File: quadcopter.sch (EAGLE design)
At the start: 0 parts

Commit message: Beginning to copy red board design
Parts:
- added C1: 1uF, quadparts_prebuilt:CAPACITOR-NP_SMD-2012-0805_CERAMIC-1UF
- added C4: 100uF, quadparts_prebuilt:CAPACITOR-POL_SMD-7043-D_TANTALUM-220UF
- added D1: 20V-500MA, quadparts_prebuilt:DIODE-SCHOTTKY_SMD-SOD123
- added R1, R2: 10K, quadparts_prebuilt:RESISTOR_SMD-2012-0805-10K
- added U$1: MOTOR_PADS, quadparts_prebuilt:MOTOR_PADS
- added U$2: MOSFET_20V, quadparts:MOSFET_20V
- added U1: ATMEGA128RFA1, quadparts_prebuilt:ATMEGA128RFA1
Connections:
- new net FILTERED: R1.2, R2.2, U$2.P-G
- new net FLYBACK: D1.A, U$1.V-, U$2.P-D
- new net GND: C1.2, C4.-, R2.1, U$2.P-S
- new net MISO: U1.PB3(MISO/PDO/PCINT3)
- new net MOSI: U1.PB2(MOSI/PDI/PCINT2)
- new net N$1: U1.EVDD
- new net N$10: U1.AVDD
- new net N$11: U1.DVDD
- new net N$12: U1.XTAL1
- new net N$13: U1.XTAL2
- new net N$14: U1.CLKI
- new net N$15: U1.AREF
- new net N$16: U1.PF0(ADC0)
- new net N$17: U1.PF1(ADC1)
- new net N$18: U1.PF2(ADC2/DIG2)
- new net N$19: U1.PF3(ADC3/DIG4)
- new net N$2: U1.DEVDD
- new net N$20: U1.PF4(ADC4/TCK)
- new net N$21: U1.PF5(ADC5/TMS)
- new net N$22: U1.PF6(ADC6/TDO)
- new net N$23: U1.PF7(ADC7/TDI)
- new net N$24: U1.AVSS
- new net N$25: U1.DVSS
- new net N$3: U1.RSTN
- new net N$4: U1.RSTON
- new net N$46: U1.PE4(OC3B/INT4)
- new net N$48: U1.PE6(T3/INT6)
- new net N$49: U1.PE7(ICP3/INT7/CLKO)
- new net N$5: U1.TST
- new net N$50: U1.PG0(DIG3)
- new net N$51: U1.PG1(DIG1)
- new net N$52: U1.PG2(AMR)
- new net N$53: U1.PG3(TOSC2)
- new net N$54: U1.PG4(TOSC1)
- new net N$55: U1.PG5(OC0B)
- new net N$6: U1.RFP
- new net N$7: U1.RFN
- new net N$8: U1.AVSS_RFP
- new net N$9: U1.AVSS_RFN
- new net PB4: U1.PB4(OC2A/PCINT4)
- new net PB5: U1.PB5(OC1A/PCINT5)
- new net PB6: U1.PB6(OC1B/PCINT6)
- new net PB7: U1.PB7(OC0A/OC1C/PCINT7)
- new net PD4: U1.PD4(ICP1)
- new net PD5: U1.PD5(XCK1)
- new net PD6: U1.PD6(T1)
- new net PD7: U1.PD7(T0)
- new net PE2: U1.PE2(XCK0/AIN0)
- new net PE3: U1.PE3(OC3A/AIN1)
- new net PE4: U1.PE5(OC3C/INT5)
- new net PWM: C1.1, R1.1
- new net RX0: U1.PE0(RXD0/PCINT8)
- new net RX1: U1.PD2(RXD1/INT2)
- new net SCK: U1.PB1(SCK/PCINT1)
- new net SCL: U1.PD0(SCL/INT0)
- new net SDA: U1.PD1(SDA/INT1)
- new net SSN: U1.PB0(SSN/PCINT0)
- new net TX0: U1.PE1(TXD0)
- new net TX1: U1.PD3(TXD1/INT3)
- new net VCC: C4.+, D1.C, U$1.V+
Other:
- note added: "Filter"
- note added: "Flyback"

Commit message: Added necessary components from red board design
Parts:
- added B1: BALUN0805, quadparts_prebuilt:BALUN0805
- added C10: 0.75pF, quadparts_prebuilt:CAPACITOR-NP_SMD-2012-0805_CERAMIC-0.75PF
- added C11, C12, C7, C8: 1uF, quadparts_prebuilt:CAPACITOR-NP_SMD-2012-0805_CERAMIC-1UF
- added C13: 0.1uF, quadparts_prebuilt:CAPACITOR-NP_SMD-2012-0805_CERAMIC-0.1UF
- added C2, C3, C5, C6: 12pF, quadparts_prebuilt:CAPACITOR-NP_SMD-2012-0805_CERAMIC-12PF
- added C9: 22pF, quadparts_prebuilt:CAPACITOR-NP_SMD-2012-0805_CERAMIC-22PF
- added D2, D3: green, quadparts_prebuilt:DIODE-LED_SMD-2012-0805-GREEN
- added J1: AVR_SPI_PRG_6NS, quadparts_prebuilt:AVR_SPI_PRG_6NS
- added JP1: FTDI_BASICPTH, quadparts_prebuilt:FTDI_BASICPTH
- added R3, R4: 330, quadparts_prebuilt:RESISTOR_SMD-2012-0805-330
- added R5: 10K, quadparts_prebuilt:RESISTOR_SMD-2012-0805-10K
- added U$3: ANTENNA2SMD5, quadparts_prebuilt:ANTENNA2SMD5
- added Y1: 32.768kHz, quadparts_prebuilt:CRYSTAL5X3
- added Y2: 16MHz, quadparts_prebuilt:CRYSTAL5X3
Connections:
- net N$14 renamed CLKI
- net N$15 renamed AREF
- net N$16 renamed A0
- net N$17 renamed A1
- net N$18 renamed A2
- net N$19 renamed A3
- net N$20 renamed A4
- net N$21 renamed A5
- net N$22 renamed A6
- net N$23 renamed A7
- net N$4 renamed RSTON
- net N$48 renamed PE6
- net N$49 renamed PE7
- net N$5 renamed TST
- net N$50 renamed PG0
- net N$51 renamed PG1
- net N$52 renamed PG2
- net N$55 renamed PG5
- removed net N$24: U1.AVSS
- removed net N$25: U1.DVSS
- removed net N$46: U1.PE4(OC3B/INT4)
- removed net N$53: U1.PG3(TOSC2)
- removed net N$54: U1.PG4(TOSC1)
- removed net VCC: C4.+, D1.C, U$1.V+
- new net 3V: C11.1, C12.1, C4.+, D1.C, J1.2, R5.2, U$1.V+, U1.DEVDD, U1.EVDD
- new net N$14: J1.1
- new net N$15: J1.3
- new net N$16: J1.5
- new net N$19: J1.6
- new net N$4: C5.1, U1.XTAL2, Y2.2
- new net N$5: C6.1, U1.XTAL1, Y2.1
- new net PE5: U1.PE5(OC3C/INT5)
- new net RESET: C13.2, R5.1, U1.RSTN
- net GND: now also B1.GND@5, C10.2, C11.2, C12.2, C2.2, C3.2, C5.2, C6.2, C7.2, C8.2, C9.2, D2.C, D3.C, JP1.6, U1.AVSS, U1.AVSS_RFN, U1.AVSS_RFP, U1.DVSS
- net MOSI: now also J1.4
- net N$1: now also C2.1, U1.PG4(TOSC1), Y1.1; no longer U1.EVDD
- net N$10: now also B1.OUT2, U1.RFN; no longer U1.AVDD
- net N$11: now also B1.GND@2, C9.1; no longer U1.DVDD
- net N$12: now also B1.IN, C10.1, U$3.SIGNAL; no longer U1.XTAL1
- net N$13: now also C13.1, JP1.1; no longer U1.XTAL2
- net N$2: now also C3.1, U1.PG3(TOSC2), Y1.2; no longer U1.DEVDD
- net N$3: now also D2.A, R3.1; no longer U1.RSTN
- net N$6: now also D3.A, R4.1; no longer U1.RFP
- net N$7: now also C7.1, U1.DVDD; no longer U1.RFN
- net N$8: now also C8.1, U1.AVDD; no longer U1.AVSS_RFP
- net N$9: now also B1.OUT1, U1.RFP; no longer U1.AVSS_RFN
- net PB6: now also R4.2
- net PB7: now also R3.2
- net PE4: now also U1.PE4(OC3B/INT4); no longer U1.PE5(OC3C/INT5)
- net RX0: now also JP1.3
- net TX0: now also JP1.2
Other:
- moved on the sheet: C1, C4, D1, R1, R2, U$1, U$2, U1

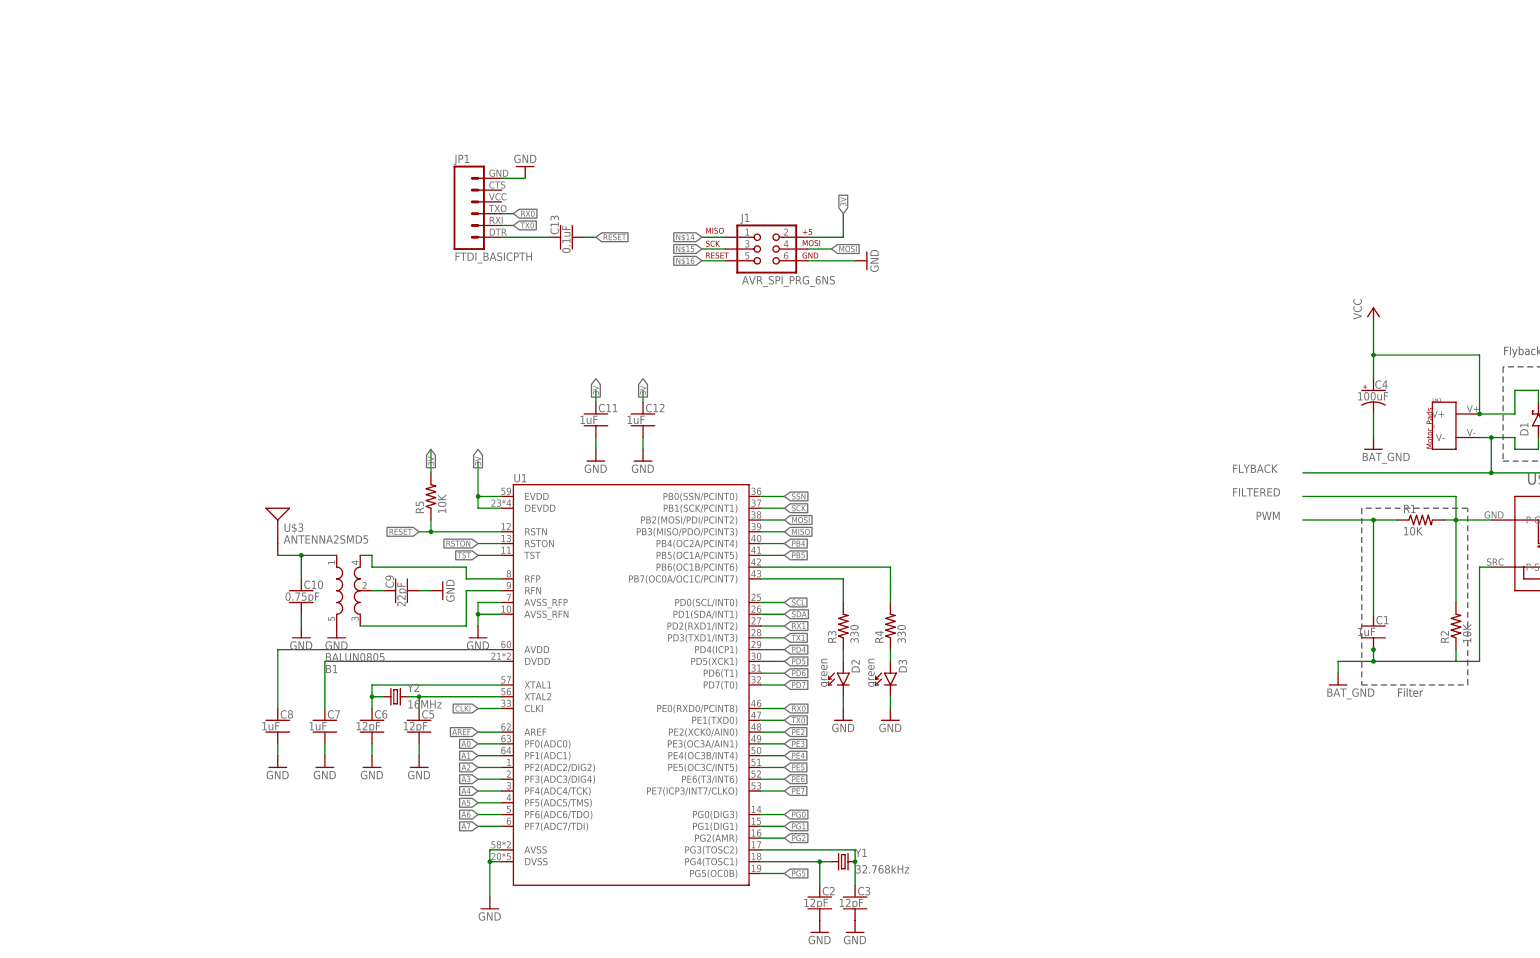
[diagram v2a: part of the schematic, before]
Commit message: Added power supply, FTDI and debugging headers, misc. fixes.
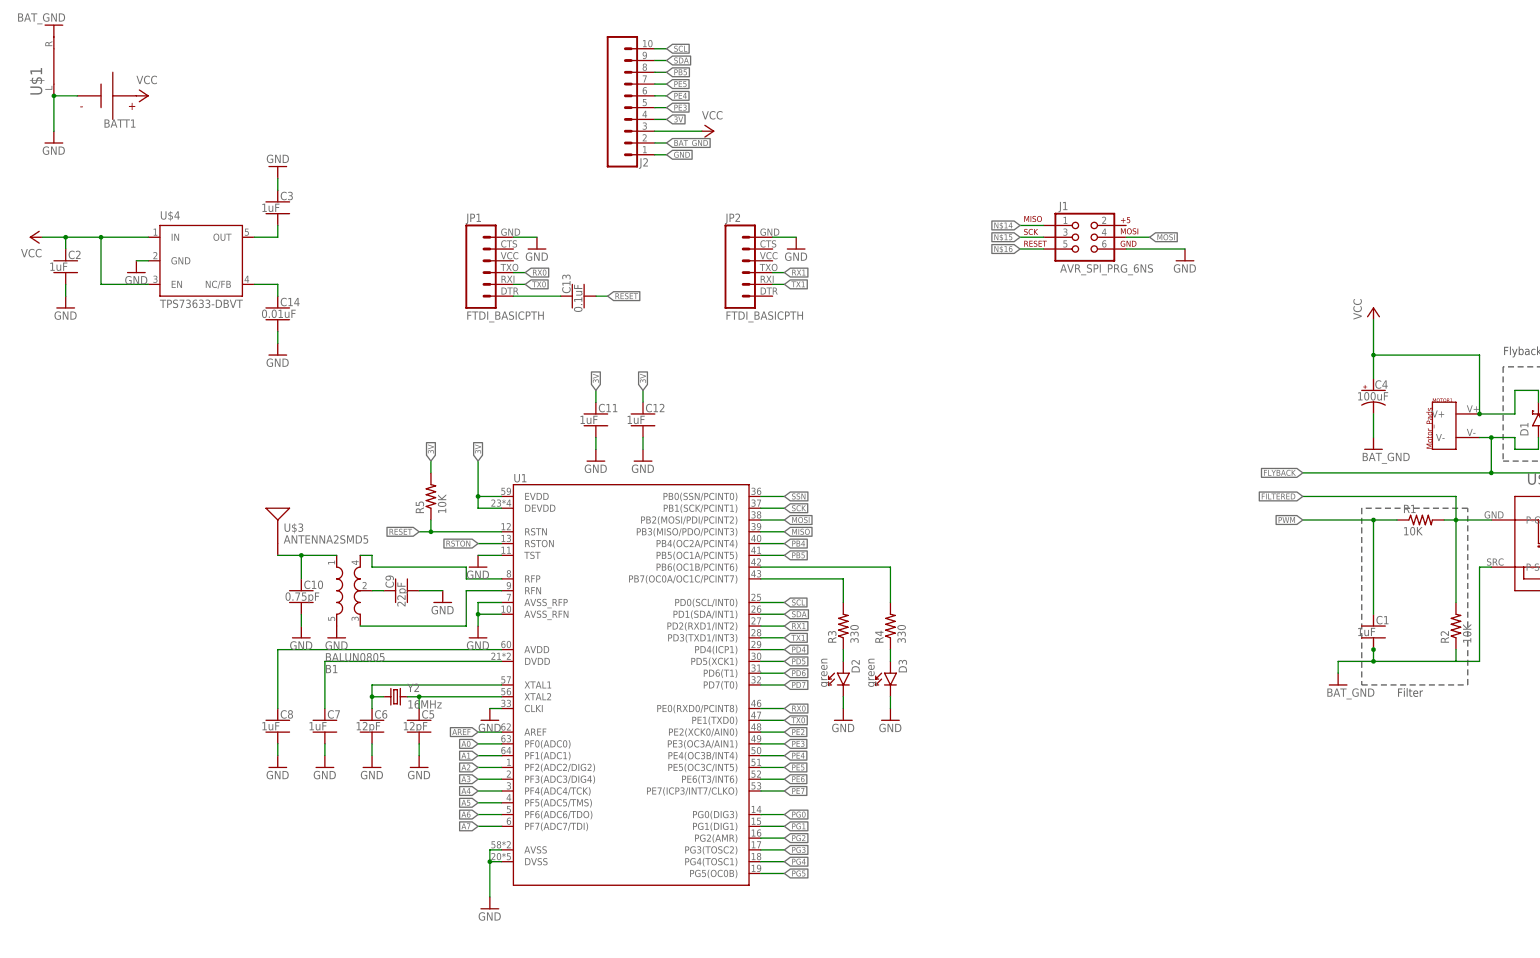
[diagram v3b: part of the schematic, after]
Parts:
- removed Y1: 32.768kHz, quadparts_prebuilt:CRYSTAL5X3
- added BATT1: BATTERY-HUBSAN-W/HOLDER, quadparts_prebuilt:BATTERY-HUBSAN-W/HOLDER
- added C14: 0.01uF, quadparts_prebuilt:CAPACITOR-NP_SMD-2012-0805_CERAMIC-0.01UF
- added J2: (no value), quadparts_prebuilt:SIP-10_TH-254X10
- added JP2: FTDI_BASICPTH, quadparts_prebuilt:FTDI_BASICPTH
- added MOTOR1: MOTOR_PADS, quadparts_prebuilt:MOTOR_PADS
- added U$4: TPS73633-DBVT, quadparts_prebuilt:TPS73633-DBVT
- C2, C3: value 12pF -> 1uF; device quadparts_prebuilt:CAPACITOR-NP_SMD-2012-0805_CERAMIC-12PF -> quadparts_prebuilt:CAPACITOR-NP_SMD-2012-0805_CERAMIC-1UF
- U$1: value MOTOR_PADS -> NET_BRIDGE; device quadparts_prebuilt:MOTOR_PADS -> quadparts:NET_BRIDGE
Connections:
- removed net CLKI: U1.CLKI
- removed net N$19: J1.6
- removed net TST: U1.TST
- new net BAT_GND: J2.2, U$1.R
- new net PG3: U1.PG3(TOSC2)
- new net PG4: U1.PG4(TOSC1)
- new net VCC: BATT1.P, C2.1, J2.3, U$4.EN, U$4.IN
- net 3V: now also J2.4, MOTOR1.V+; no longer J1.2, U$1.V+
- net FLYBACK: now also MOTOR1.V-; no longer U$1.V-
- net GND: now also BATT1.N, C14.2, C3.1, J1.6, J2.1, JP2.6, U$1.L, U$4.GND, U1.CLKI, U1.TST; no longer C3.2
- net N$1: now also C14.1, U$4.NC/FB; no longer C2.1, U1.PG4(TOSC1), Y1.1
- net N$2: now also C3.2, U$4.OUT; no longer C3.1, U1.PG3(TOSC2), Y1.2
- net PB5: now also J2.8
- net PE3: now also J2.5
- net PE4: now also J2.6
- net PE5: now also J2.7
- net RX1: now also JP2.3
- net SCL: now also J2.10
- net SDA: now also J2.9
- net TX1: now also JP2.2
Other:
- moved on the sheet: C13, C2, C3, J1, JP1

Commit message: Added battery disconnect, replicated motor controller w/ pwm, misc fixes.
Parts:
- added C15, C17, C19: 1uF, quadparts_prebuilt:CAPACITOR-NP_SMD-2012-0805_CERAMIC-1UF
- added C16, C18, C20: 100uF, quadparts_prebuilt:CAPACITOR-POL_SMD-7043-D_TANTALUM-220UF
- added D4, D5, D6: 20V-500MA, quadparts_prebuilt:DIODE-SCHOTTKY_SMD-SOD123
- added J3: (no value), quadparts:MALE_HEADER_2POS-2X1-0.1IN
- added MOTOR2, MOTOR3, MOTOR4: MOTOR_PADS, quadparts_prebuilt:MOTOR_PADS
- added R10, R11, R6, R7, R8, R9: 10K, quadparts_prebuilt:RESISTOR_SMD-2012-0805-10K
- added U$5, U$6, U$7: MOSFET_20V, quadparts:MOSFET_20V
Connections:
- removed net N$2: C3.2, U$4.OUT
- removed net PWM: C1.1, R1.1
- new net N$17: BATT1.P, J3.1
- net 3V: now also C16.+, C18.+, C20.+, C3.2, D4.C, D5.C, D6.C, MOTOR2.V+, MOTOR3.V+, MOTOR4.V+, U$4.OUT
- net FILTERED: now also R10.2, R11.2, R6.2, R7.2, R8.2, R9.2, U$5.P-G, U$6.P-G, U$7.P-G
- net FLYBACK: now also D4.A, D5.A, D6.A, MOTOR2.V-, MOTOR3.V-, MOTOR4.V-, U$5.P-D, U$6.P-D, U$7.P-D
- net GND: now also C15.2, C16.-, C17.2, C18.-, C19.2, C20.-, R11.1, R7.1, R9.1, U$5.P-S, U$6.P-S, U$7.P-S
- net PB5: now also C15.1, R6.1
- net PE3: now also C1.1, R1.1
- net PE4: now also C19.1, R10.1
- net PE5: now also C17.1, R8.1
- net VCC: now also J3.2; no longer BATT1.P
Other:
- moved on the sheet: B1, C1, C10, C11, C12, C4, C5, C6, C7, C8, C9, D1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

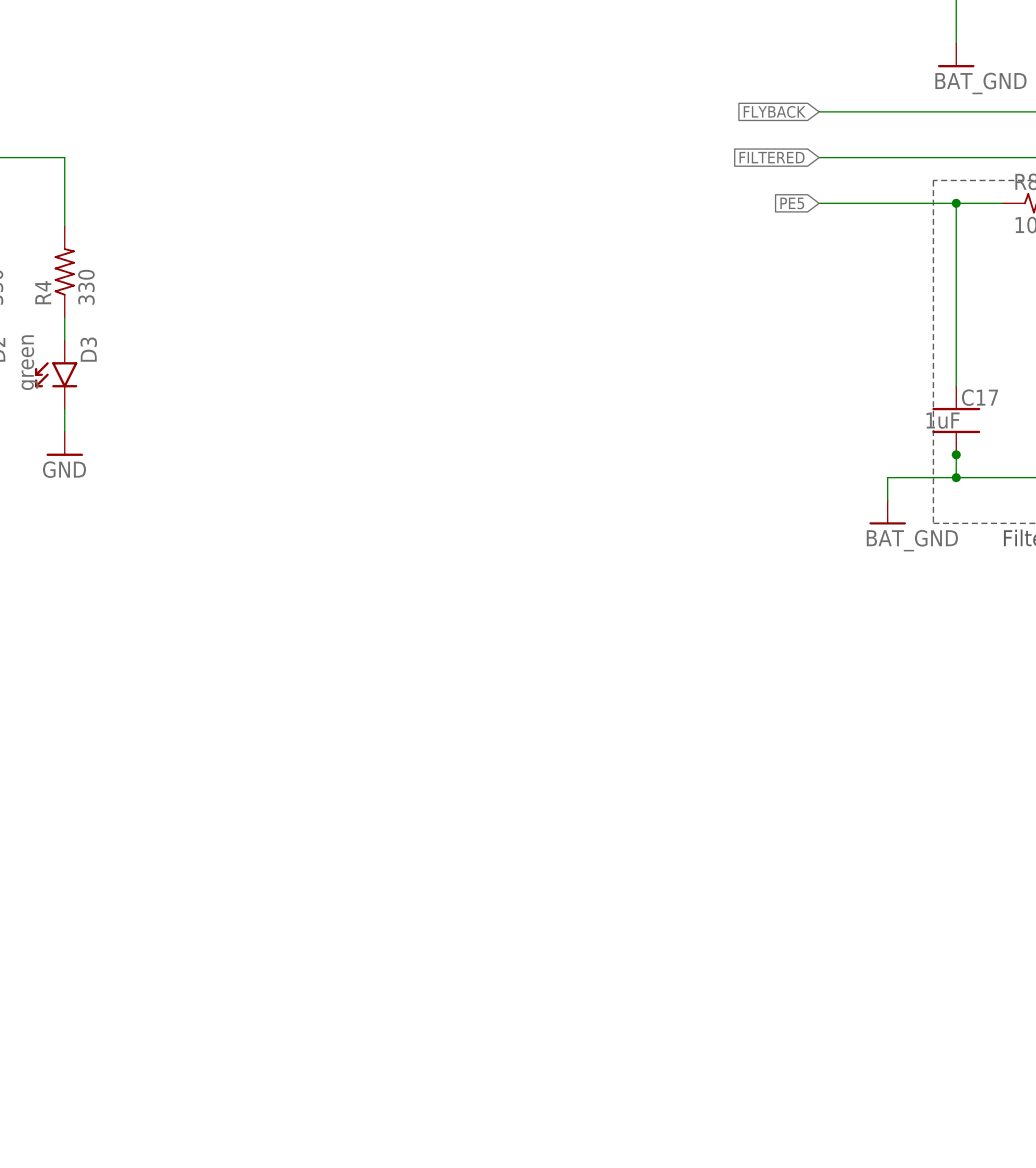
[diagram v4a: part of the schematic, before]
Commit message: added IMU to quadcopter
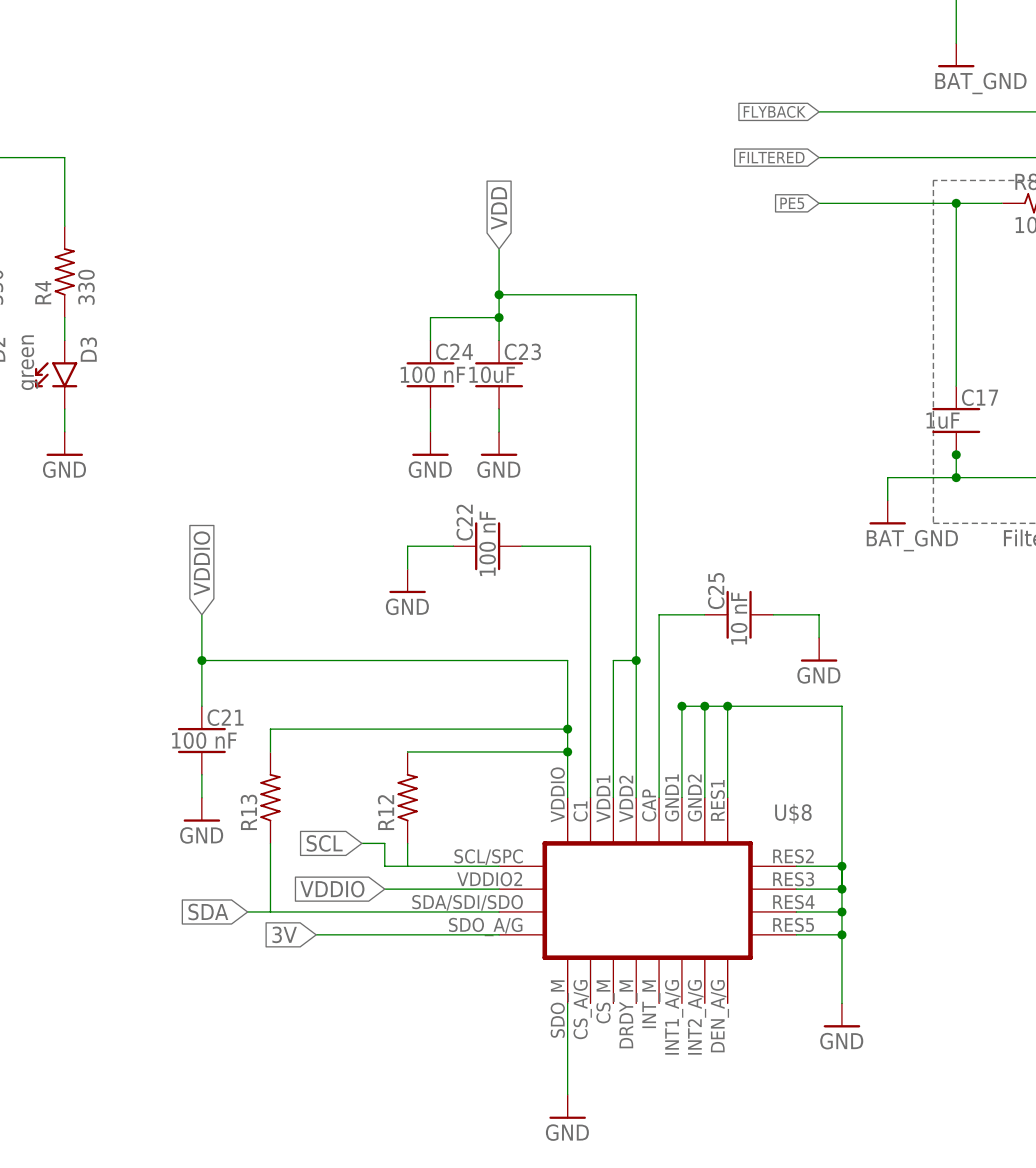
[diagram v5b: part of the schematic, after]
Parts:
- added C21, C22, C24: 100 nF, quadparts_prebuilt:CAPACITOR-NP_SMD-2012-0805_CERAMIC
- added C23: 10uF, quadparts_prebuilt:CAPACITOR-NP_SMD-2012-0805_CERAMIC-10UF
- added C25: 10 nF, quadparts_prebuilt:CAPACITOR-NP_SMD-2012-0805_CERAMIC
- added R12, R13: (no value), quadparts_prebuilt:RESISTOR_SMD-2012-0805
- added U$8: IMU_9AXIS, quadparts:IMU_9AXIS
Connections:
- new net N$20: C25.1, U$8.CAP
- new net N$23: C22.2, U$8.C1
- new net VDD: C23.1, C24.1, U$8.VDD1, U$8.VDD2
- new net VDDIO: C21.1, R12.2, R13.2, U$8.VDDIO1, U$8.VDDIO2
- net 3V: now also U$8.SDO_A/G
- net GND: now also C21.2, C22.1, C23.2, C24.2, C25.2, U$8.GND1, U$8.GND2, U$8.RES1, U$8.RES2, U$8.RES3, U$8.RES4, U$8.RES5, U$8.SDO_M
- net SCL: now also R12.1, U$8.SCL/SPC
- net SDA: now also R13.1, U$8.SDA/SDI/SDO
